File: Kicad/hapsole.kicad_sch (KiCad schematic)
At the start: 64 parts, among them J1 2171790001, J2 Conn_01x02_Socket, J3 Conn_01x02_Socket, Q1 PMOS, SW1 SW_SPST, U1 DA7281-00FV2, U2 DA7281-00FV2, U3 nRF52840, U4 LSM6DS3TR-C, U5 BQ25100YFPR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

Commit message: Resized and rearranged components placement
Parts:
- U3: footprint Arjun_Custom:NRF52840 -> Package_DFN_QFN:Nordic_AQFN-73-1EP_7x7mm_P0.5mm
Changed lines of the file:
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@@
 	)
 	(junction
+		(at 175.26 250.19)
+		(diameter 0)
+		(color 0 0 0 0)
+	)
+	(junction
 		(at 295.91 170.18)
 		(diameter 0)
@@
 	)
 	(junction
-		(at 175.26 250.19)
-		(diameter 0)
-		(color 0 0 0 0)
-	)
-	(junction
 		(at 336.55 43.18)
 		(diameter 0)
@@
 	)
 	(symbol
+		(lib_id "MCU_Nordic:nRF52840")
+		(at 175.26 179.07 0)
+		(unit 1)
+		(exclude_from_sim no)
+		(in_bom yes)
+		(on_board yes)
+		(dnp no)
+		(fields_autoplaced yes)
+		(property "Reference" "U3"
+			(at 179.9433 247.65 0)
+			(effects
+				(font
+					(size 1.27 1.27)
+				)
+				(justify left)
+			)
+		)
+		(property "Value" "nRF52840"
+			(at 179.9433 250.19 0)
+			(effects
+				(font
+					(size 1.27 1.27)
+				)
+				(justify left)
+			)
+		)
+		(property "Footprint" "Package_DFN_QFN:Nordic_AQFN-73-1EP_7x7mm_P0.5mm"
+			(at 175.26 252.73 0)
+			(effects
+				(font
+					(size 1.27 1.27)
+				)
+				(hide yes)
+			)
+		)
+		(property "Datasheet" "http://infocenter.nordicsemi.com/topic/com.nordic.infocenter.nrf52/dita/nrf52/chips/nrf52840.html"
+			(at 158.75 130.81 0)
+			(effects
+				(font
+					(size 1.27 1.27)
+				)
+				(hide yes)
+			)
+		)
+		(property "Description" "Multiprotocol BLE/ANT/2.4 GHz/802.15.4 Cortex-M4F SoC, AQFN-73"
+			(at 175.26 179.07 0)
+			(effects
+				(font
+					(size 1.27 1.27)
+				)
+				(hide yes)
+			)
+		)
+		(pin "D23"
+		)
+		(pin "AD23"
+		)
+		(pin "AB2"
+		)
+		(pin "AA24"
+		)
+		(pin "C1"
+		)
+		(pin "AC13"
+		)
+		(pin "AD14"
+		)
+		(pin "B7"
+		)
+		(pin "W1"
+		)
+		(pin "A12"
+		)
+		(pin "A23"
+		)
+		(pin "B1"
+		)
+		(pin "H23"
+		)
+		(pin "Y2"
+		)
+		(pin "F23"
+		)
+		(pin "A18"
+		)
+		(pin "AD2"
+		)
+		(pin "N24"
+		)
+		(pin "B3"
+		)
+		(pin "AC15"
+		)
+		(pin "AC24"
+		)
+		(pin "B5"
+		)
+		(pin "E24"
+		)
+		(pin "B24"
+		)
+		(pin "AC5"
+		)
+		(pin "A22"
+		)
+		(pin "EP"
+		)
+		(pin "D2"
+		)
+		(pin "F2"
+		)
+		(pin "B13"
+		)
+		(pin "J1"
+		)
+		(pin "L1"
+		)
+		(pin "M2"
+		)
+		(pin "N1"
+		)
+		(pin "L24"
+		)
+		(pin "J24"
+		)
+		(pin "T2"
+		)
+		(pin "U1"
+		)
+		(pin "AD8"
+		)
+		(pin "AC9"
+		)
+		(pin "AD10"
+		)
+		(pin "K2"
+		)
+		(pin "AC11"
+		)
+		(pin "AD12"
+		)
+		(pin "AC21"
+		)
+		(pin "G1"
+		)
+		(pin "B11"
+		)
+		(pin "AD22"
+		)
+		(pin "A10"
+		)
+		(pin "Y23"
+		)
+		(pin "V23"
+		)
+		(pin "U24"
+		)
+		(pin "T23"
+		)
+		(pin "AD18"
+		)
+		(pin "W24"
+		)
+		(pin "A8"
+		)
+		(pin "AC17"
+		)
+		(pin "AD20"
+		)
+		(pin "P23"
+		)
+		(pin "B9"
+		)
+		(pin "R24"
+		)
+		(pin "H2"
+		)
+		(pin "AC19"
+		)
+		(pin "AD16"
+		)
+		(pin "AD4"
+		)
+		(pin "AD6"
+		)
+		(pin "B17"
+		)
+		(pin "P2"
+		)
+		(pin "A20"
+		)
+		(pin "B19"
+		)
+		(pin "B15"
+		)
+		(pin "R1"
+		)
+		(pin "A14"
+		)
+		(pin "A16"
+		)
+		(instances
+			(project ""
+				(path "/85cf9212-affa-4e9a-a568-1311b90cc1d6"
+					(reference "U3")
+					(unit 1)
+				)
+			)
+		)
+	)
+	(symbol
 		(lib_id "Device:R")
 		(at 351.79 236.22 270)
@@
 					(unit 1)
 				)
-			)
-		)
-	)
-	(symbol
-		(lib_id "MCU_Nordic:nRF52840")
-		(at 175.26 179.07 0)
-		(unit 1)
-		(exclude_from_sim no)
-		(in_bom yes)
-		(on_board yes)
-		(dnp no)
-		(fields_autoplaced yes)
-		(property "Reference" "U3"
-			(at 179.9433 247.65 0)
-			(effects
-				(font
-					(size 1.27 1.27)
-				)
-				(justify left)
-			)
-		)
-		(property "Value" "nRF52840"
-			(at 179.9433 250.19 0)
-			(effects
-				(font
-					(size 1.27 1.27)
-				)
-				(justify left)
-			)
-		)
-		(property "Footprint" "Arjun_Custom:NRF52840"
-			(at 175.26 252.73 0)
-			(effects
-				(font
-					(size 1.27 1.27)
-				)
-				(hide yes)
-			)
-		)
-		(property "Datasheet" "http://infocenter.nordicsemi.com/topic/com.nordic.infocenter.nrf52/dita/nrf52/chips/nrf52840.html"
-			(at 158.75 130.81 0)
-			(effects
-				(font
-					(size 1.27 1.27)
-				)
-				(hide yes)
-			)
-		)
-		(property "Description" "Multiprotocol BLE/ANT/2.4 GHz/802.15.4 Cortex-M4F SoC, AQFN-73"
-			(at 175.26 179.07 0)
-			(effects
-				(font
-					(size 1.27 1.27)
-				)
-				(hide yes)
-			)
-		)
-		(pin "A16"
-		)
-		(pin "A14"
-		)
-		(pin "B15"
-		)
-		(pin "AD6"
-		)
-		(pin "B17"
-		)
-		(pin "B19"
-		)
-		(pin "AD4"
-		)
-		(pin "A23"
-		)
-		(pin "A18"
-		)
-		(pin "AA24"
-		)
-		(pin "D23"
-		)
-		(pin "AC13"
-		)
-		(pin "H23"
-		)
-		(pin "AC24"
-		)
-		(pin "B24"
-		)
-		(pin "C1"
-		)
-		(pin "A22"
-		)
-		(pin "AD14"
-		)
-		(pin "AB2"
-		)
-		(pin "K2"
-		)
-		(pin "B5"
-		)
-		(pin "N24"
-		)
-		(pin "E24"
-		)
-		(pin "AC5"
-		)
-		(pin "T2"
-		)
-		(pin "EP"
-		)
-		(pin "Y2"
-		)
-		(pin "D2"
-		)
-		(pin "F23"
-		)
-		(pin "B13"
-		)
-		(pin "B1"
-		)
-		(pin "A12"
-		)
-		(pin "AD23"
-		)
-		(pin "W1"
-		)
-		(pin "B7"
-		)
-		(pin "B3"
-		)
-		(pin "J1"
-		)
-		(pin "AD2"
-		)
-		(pin "F2"
-		)
-		(pin "L1"
-		)
-		(pin "M2"
-		)
-		(pin "N1"
-		)
-		(pin "L24"
-		)
-		(pin "J24"
-		)
-		(pin "AD20"
-		)
-		(pin "V23"
-		)
-		(pin "T23"
-		)
-		(pin "A8"
-		)
-		(pin "AC9"
-		)
-		(pin "A20"
-		)
-		(pin "R1"
-		)
-		(pin "AC21"
-		)
-		(pin "AC15"
-		)
-		(pin "W24"
-		)
-		(pin "U1"
-		)
-		(pin "AD10"
-		)
-		(pin "H2"
-		)
-		(pin "AC17"
-		)
-		(pin "AD16"
-		)
-		(pin "B11"
-		)
-		(pin "AD12"
-		)
-		(pin "A10"
-		)
-		(pin "AD8"
-		)
-		(pin "G1"
-		)
-		(pin "AC11"
-		)
-		(pin "AC19"
-		)
-		(pin "B9"
-		)
-		(pin "AD18"
-		)
-		(pin "AD22"
-		)
-		(pin "Y23"
-		)
-		(pin "U24"
-		)
-		(pin "R24"
-		)
-		(pin "P23"
-		)
-		(pin "P2"
-		)
-		(instances
-			(project ""
-				(path "/85cf9212-affa-4e9a-a568-1311b90cc1d6"
-					(reference "U3")
-					(unit 1)
-				)

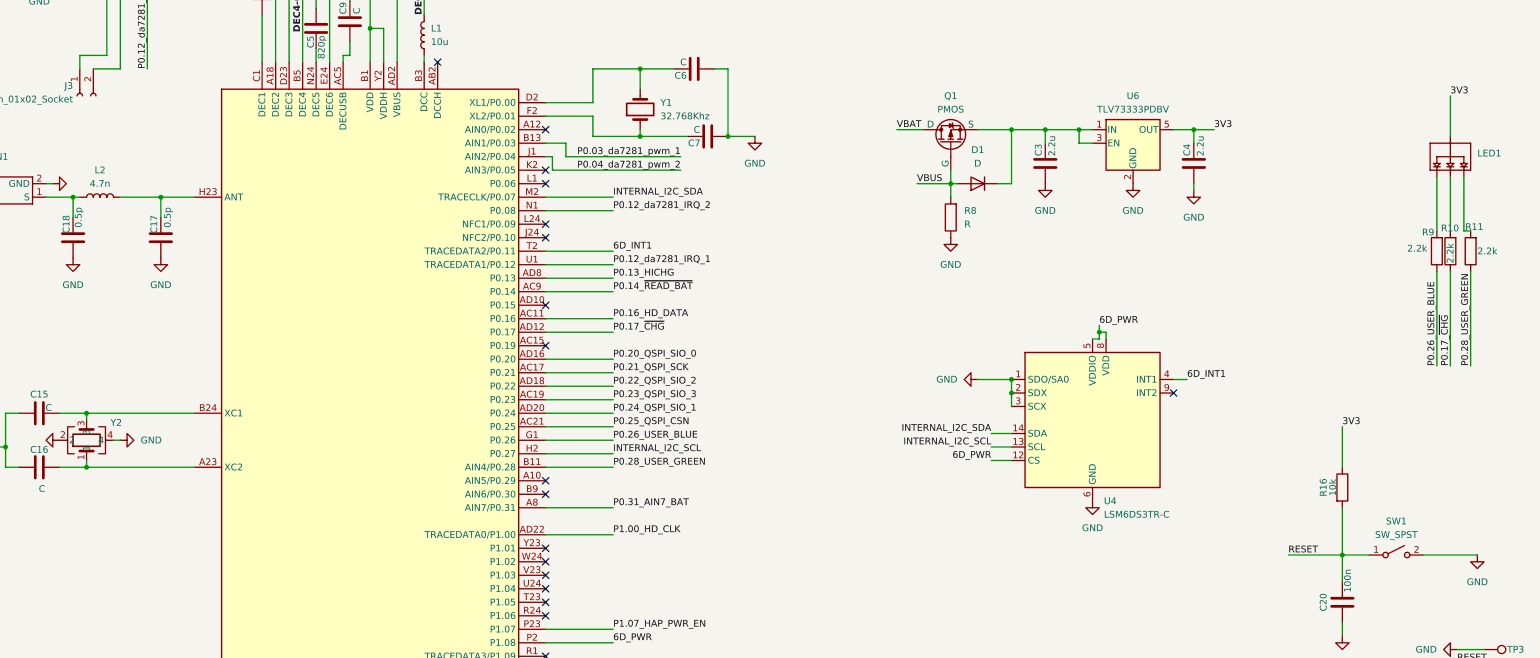
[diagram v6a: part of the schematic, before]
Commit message: Deleted the pcb design and start from the scratch
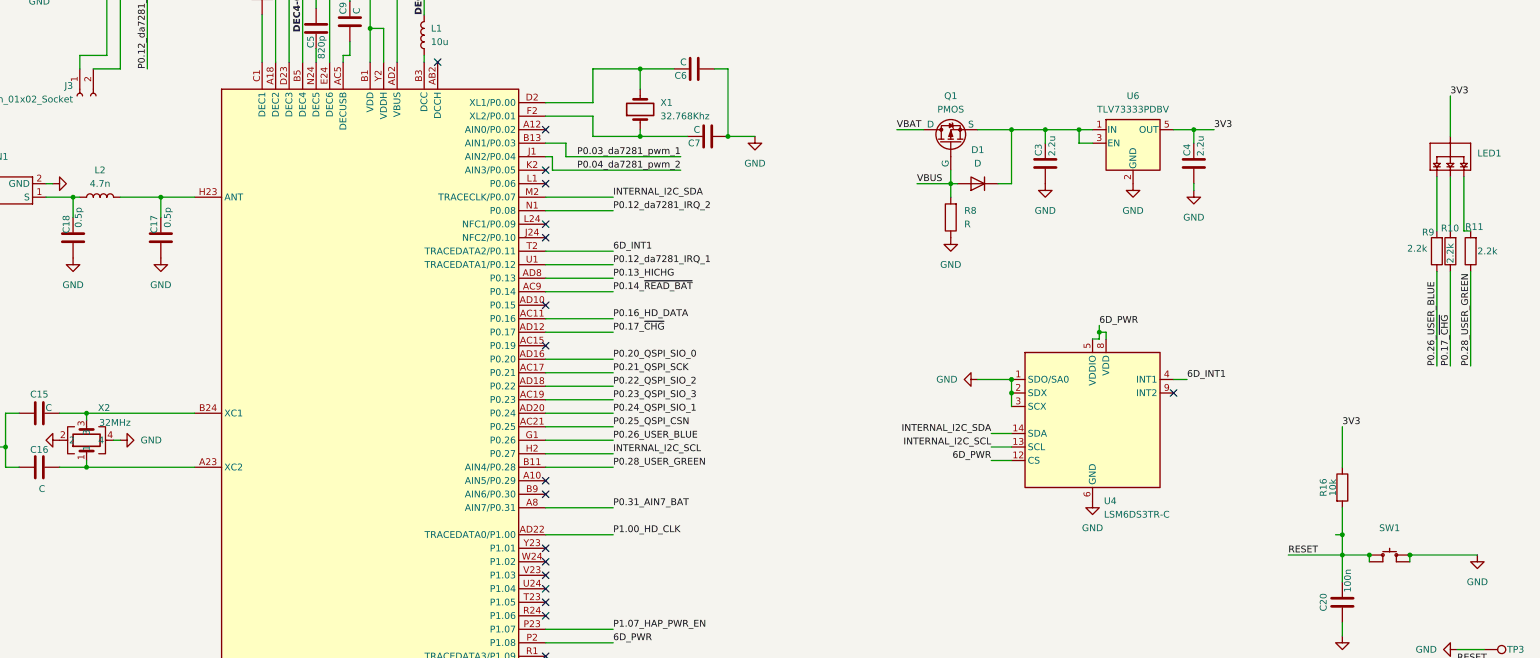
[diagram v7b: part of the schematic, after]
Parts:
- removed SW1: SW_SPST, Arjun_Custom:SW_EVP-AWED4A, symbol Switch:SW_SPST
- added SW1: ~, Hapsole_Custom:DPST, symbol Arjun_Custom:DPST
- AN1: footprint Arjun_Custom:Ant -> Hapsole_Custom:ANT
- J1: footprint Arjun_Custom:MOLEX_2171790001 -> Hapsole_Custom:MOLEX_2171790001
- J2, J3: footprint Arjun_Custom:JST_S2B-ZR-SM4A-TF -> Hapsole_Custom:JST_S2B-ZR-SM4A-TF
- LED1: footprint Arjun_Custom:RGB_LED_P4_1010 -> Hapsole_Custom:RGB_LED
- U1, U2: footprint Arjun_Custom:DA7281-00FV2_DIL -> Hapsole_Custom:DA7281-00FV2_DIL
- U5: footprint Arjun_Custom:BGA6N40P3X2_157X88X50N -> Hapsole_Custom:BGA6N40P3X2_157X88X50N
- X1: renamed from Y1; footprint Arjun_Custom:XTAL_FC-135_32.7680KA-A0 -> Hapsole_Custom:FC135
- X2: renamed from Y2; value ~ -> 32MHz; footprint Arjun_Custom:XTAL_ABM12W-40.0000MHZ-6-D1X-T3 -> Hapsole_Custom:XC
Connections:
- net GND: now also SW1.2 (B0), SW1.4 (B1)
- net RESET: now also SW1.1 (A0), SW1.3 (A1)
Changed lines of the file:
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@@
 	)
 	(junction
+		(at 358.14 196.85)
+		(diameter 0)
+		(color 0 0 0 0)
+	)
+	(junction
 		(at 180.34 82.55)
 		(diameter 0)
@@
 	)
 	(junction
+		(at 363.22 200.66)
+		(diameter 0)
+		(color 0 0 0 0)
+	)
+	(junction
 		(at 121.92 184.15)
 		(diameter 0)
@@
 	)
 	(junction
+		(at 370.84 200.66)
+		(diameter 0)
+		(color 0 0 0 0)
+	)
+	(junction
 		(at 242.57 121.92)
 		(diameter 0)
@@
 	(wire
 		(pts
+			(xy 370.84 200.66) (xy 383.54 200.66)
+		)
+		(stroke
+			(width 0)
+			(type default)
+		)
+	)
+	(wire
+		(pts
 			(xy 214.63 46.99) (xy 218.44 46.99)
 		)
@@
 	(wire
 		(pts
+			(xy 363.22 200.66) (xy 363.22 201.93)
+		)
+		(stroke
+			(width 0)
+			(type default)
+		)
+	)
+	(wire
+		(pts
 			(xy 292.1 182.88) (xy 295.91 182.88)
 		)
@@
 	(wire
 		(pts
+			(xy 358.14 196.85) (xy 358.14 200.66)
+		)
+		(stroke
+			(width 0)
+			(type default)
+		)
+	)
+	(wire
+		(pts
 			(xy 121.92 184.15) (xy 142.24 184.15)
 		)
@@
 	(wire
 		(pts
+			(xy 370.84 200.66) (xy 370.84 201.93)
+		)
+		(stroke
+			(width 0)
+			(type default)
+		)
+	)
+	(wire
+		(pts
 			(xy 160.02 86.36) (xy 160.02 78.74)
 		)
@@
 	(wire
 		(pts
+			(xy 356.87 196.85) (xy 358.14 196.85)
+		)
+		(stroke
+			(width 0)
+			(type default)
+		)
+	)
+	(wire
+		(pts
 			(xy 326.39 120.65) (xy 330.2 120.65)
 		)
@@
 	(wire
 		(pts
-			(xy 358.14 191.77) (xy 358.14 200.66)
+			(xy 358.14 191.77) (xy 358.14 196.85)
 		)
 		(stroke
@@
 	(wire
 		(pts
-			(xy 383.54 200.66) (xy 373.38 200.66)
-		)
-		(stroke
-			(width 0)
-			(type default)
-		)
-	)
-	(wire
-		(pts
 			(xy 157.48 78.74) (xy 157.48 80.01)
 		)
@@
 	)
 	(symbol
-		(lib_id "Switch:SW_SPST")
-		(at 368.3 200.66 0)
-		(unit 1)
-		(exclude_from_sim no)
-		(in_bom yes)
-		(on_board yes)
-		(dnp no)
-		(fields_autoplaced yes)
-		(property "Reference" "SW1"
-			(at 368.3 194.31 0)
-			(effects
-				(font
-					(size 1.27 1.27)
-				)
-			)
-		)
-		(property "Value" "SW_SPST"
-			(at 368.3 196.85 0)
-			(effects
-				(font
-					(size 1.27 1.27)
-				)
-			)
-		)
-		(property "Footprint" "Arjun_Custom:SW_EVP-AWED4A"
-			(at 368.3 200.66 0)
-			(effects
-				(font
-					(size 1.27 1.27)
-				)
-				(hide yes)
-			)
-		)
-		(property "Datasheet" "~"
-			(at 368.3 200.66 0)
-			(effects
-				(font
-					(size 1.27 1.27)
-				)
-				(hide yes)
-			)
-		)
-		(property "Description" "Single Pole Single Throw (SPST) switch"
-			(at 368.3 200.66 0)
-			(effects
-				(font
-					(size 1.27 1.27)
-				)
-				(hide yes)
-			)
-		)
-		(pin "1"
-		)
-		(pin "2"
-		)
-		(instances
-			(project ""
-				(path "/85cf9212-affa-4e9a-a568-1311b90cc1d6"
-					(reference "SW1")
-					(unit 1)
-				)
-			)
-		)
-	)
-	(symbol
 		(lib_id "Device:R")
 		(at 321.31 27.94 90)
@@
 			)
 		)
-		(property "Footprint" "Arjun_Custom:RGB_LED_P4_1010"
+		(property "Footprint" "Hapsole_Custom:RGB_LED"
 			(at 381 125.73 0)
 			(effects
@@
 			)
 		)
-		(property "Footprint" "Arjun_Custom:DA7281-00FV2_DIL"
+		(property "Footprint" "Hapsole_Custom:DA7281-00FV2_DIL"
 			(at 128.27 68.58 0)
 			(effects
@@
 		(on_board yes)
 		(dnp no)
-		(property "Reference" "Y2"
-			(at 127.508 175.768 90)
+		(property "Reference" "X2"
+			(at 125.222 172.974 90)
 			(effects
 				(font
@@
 			)
 		)
-		(property "Value" "~"
-			(at 128.27 176.7997 90)
+		(property "Value" "32MHz"
+			(at 127.254 175.768 90)
 			(effects
 				(font
@@
 			)
 		)
-		(property "Footprint" "Arjun_Custom:XTAL_ABM12W-40.0000MHZ-6-D1X-T3"
+		(property "Footprint" "Hapsole_Custom:XC"
 			(at 121.92 179.07 0)
 			(effects
@@
 			(project ""
 				(path "/85cf9212-affa-4e9a-a568-1311b90cc1d6"
-					(reference "Y2")
+					(reference "X2")
 					(unit 1)
 				)
@@
 	)
 	(symbol
+		(lib_id "Arjun_Custom:DPST")
+		(at 367.03 198.12 0)
+		(unit 1)
+		(exclude_from_sim no)
+		(in_bom yes)
+		(on_board yes)
+		(dnp no)
+		(fields_autoplaced yes)
+		(property "Reference" "SW1"
+			(at 367.03 195.58 0)
+			(effects
+				(font
+					(size 1.27 1.27)
+				)
+			)
+		)
+		(property "Value" "~"
+			(at 367.03 198.12 0)
+			(effects
+				(font
+					(size 1.27 1.27)
+				)
+			)
+		)
+		(property "Footprint" "Hapsole_Custom:DPST"
+			(at 367.03 198.12 0)
+			(effects
+				(font
+					(size 1.27 1.27)
+				)
+				(hide yes)
+			)
+		)
+		(property "Datasheet" ""
+			(at 367.03 198.12 0)
+			(effects
+				(font
+					(size 1.27 1.27)
+				)
+				(hide yes)
+			)
+		)
+		(property "Description" ""
+			(at 367.03 198.12 0)
+			(effects
+				(font
+					(size 1.27 1.27)
+				)
+				(hide yes)
+			)
+		)
+		(pin "3"
+		)
+		(pin "1"
+		)
+		(pin "4"
+		)
+		(pin "2"
+		)
+		(instances
+			(project ""
+				(path "/85cf9212-affa-4e9a-a568-1311b90cc1d6"
+					(reference "SW1")
+					(unit 1)
+				)
+			)
+		)
+	)
+	(symbol
 		(lib_id "Device:R")
 		(at 382.27 143.51 180)
@@
 	)
 	(symbol
+		(lib_name "DA7281-00FV2_1")
 		(lib_id "Arjun_Custom:DA7281-00FV2")
 		(at 60.96 68.58 270)
@@
 			)
 		)
-		(property "Footprint" "Arjun_Custom:DA7281-00FV2_DIL"
+		(property "Footprint" "Hapsole_Custom:DA7281-00FV2_DIL"
 			(at 60.96 68.58 0)
 			(effects
@@
 			)
 		)
-		(property "Footprint" "Arjun_Custom:Ant"
+		(property "Footprint" "Hapsole_Custom:ANT"
 			(at 105.41 132.08 0)
 			(effects
@@
 			)
 		)
-		(property "Footprint" "Arjun_Custom:JST_S2B-ZR-SM4A-TF"
+		(property "Footprint" "Hapsole_Custom:JST_S2B-ZR-SM4A-TF"
 			(at 120.65 114.3 0)
 			(effects
@@
 			)
 		)
-		(property "Footprint" "Arjun_Custom:JST_S2B-ZR-SM4A-TF"
+		(property "Footprint" "Hapsole_Custom:JST_S2B-ZR-SM4A-TF"
 			(at 58.42 115.57 0)
 			(effects
@@
 		(dnp no)
 		(fields_autoplaced yes)
-		(property "Reference" "Y1"
+		(property "Reference" "X1"
 			(at 229.87 115.5699 90)
 			(effects
@@
 			)
 		)
-		(property "Footprint" "Arjun_Custom:XTAL_FC-135_32.7680KA-A0"
+		(property "Footprint" "Hapsole_Custom:FC135"
 			(at 226.06 116.84 0)
 			(effects
@@
 			(project ""
 				(path "/85cf9212-affa-4e9a-a568-1311b90cc1d6"
-					(reference "Y1")
+					(reference "X1")
 					(unit 1)
 				)
@@
 			)
 		)
-		(property "Footprint" "Arjun_Custom:BGA6N40P3X2_157X88X50N"
+		(property "Footprint" "Hapsole_Custom:BGA6N40P3X2_157X88X50N"
 			(at 236.22 46.99 0)
 			(effects
@@
 			)
 		)
-		(property "Footprint" "Arjun_Custom:MOLEX_2171790001"
+		(property "Footprint" "Hapsole_Custom:MOLEX_2171790001"
 			(at 354.33 40.64 0)
 			(effects

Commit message: finished arrangement of all components
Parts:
- U7: footprint Package_SO:SOIC-8_5.3x5.3mm_P1.27mm -> Hapsole_Custom:Untitled
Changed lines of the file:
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@@
 			)
 		)
-		(property "Footprint" "Package_SO:SOIC-8_5.3x5.3mm_P1.27mm"
+		(property "Footprint" "Hapsole_Custom:Untitled"
 			(at 49.53 243.84 0)
 			(effects
